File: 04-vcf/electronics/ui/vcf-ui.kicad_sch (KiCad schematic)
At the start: 39 parts, among them J1 Conn_02x03_Odd_Even, J2 Conn_02x02_Counter_Clockwise, J4 Conn_01x02, J5 Conn_01x06, J6 Conn_02x04_Odd_Even, U1 TL072

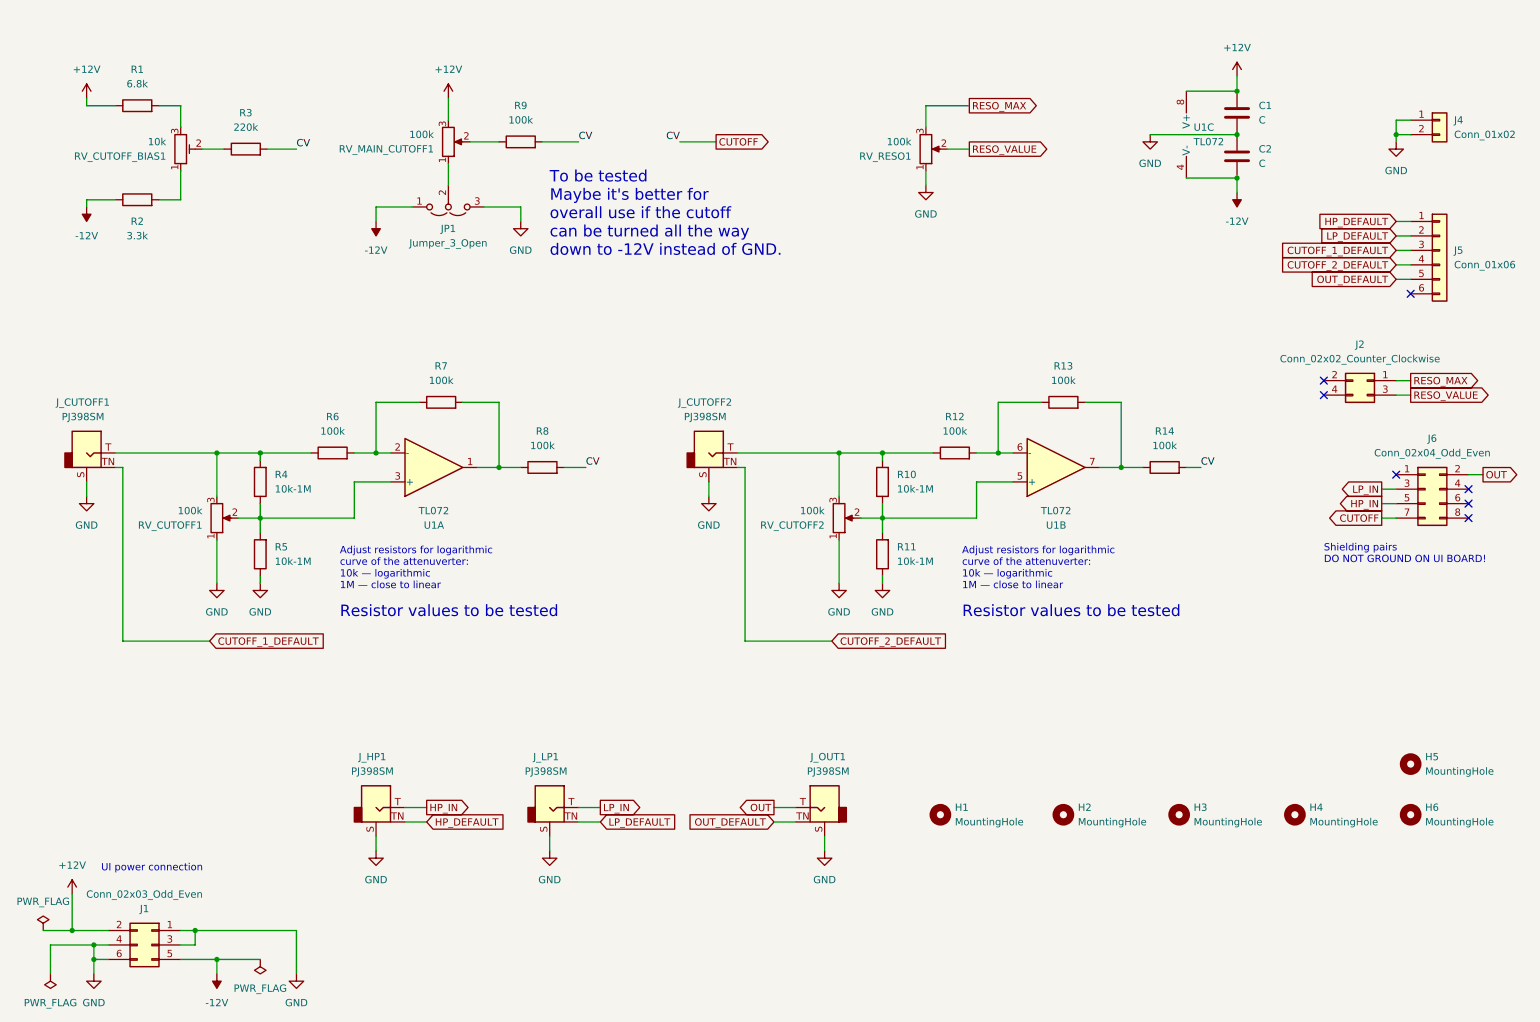
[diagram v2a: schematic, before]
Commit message: Fixed VCF v0.1 bugs - new version: v0.2
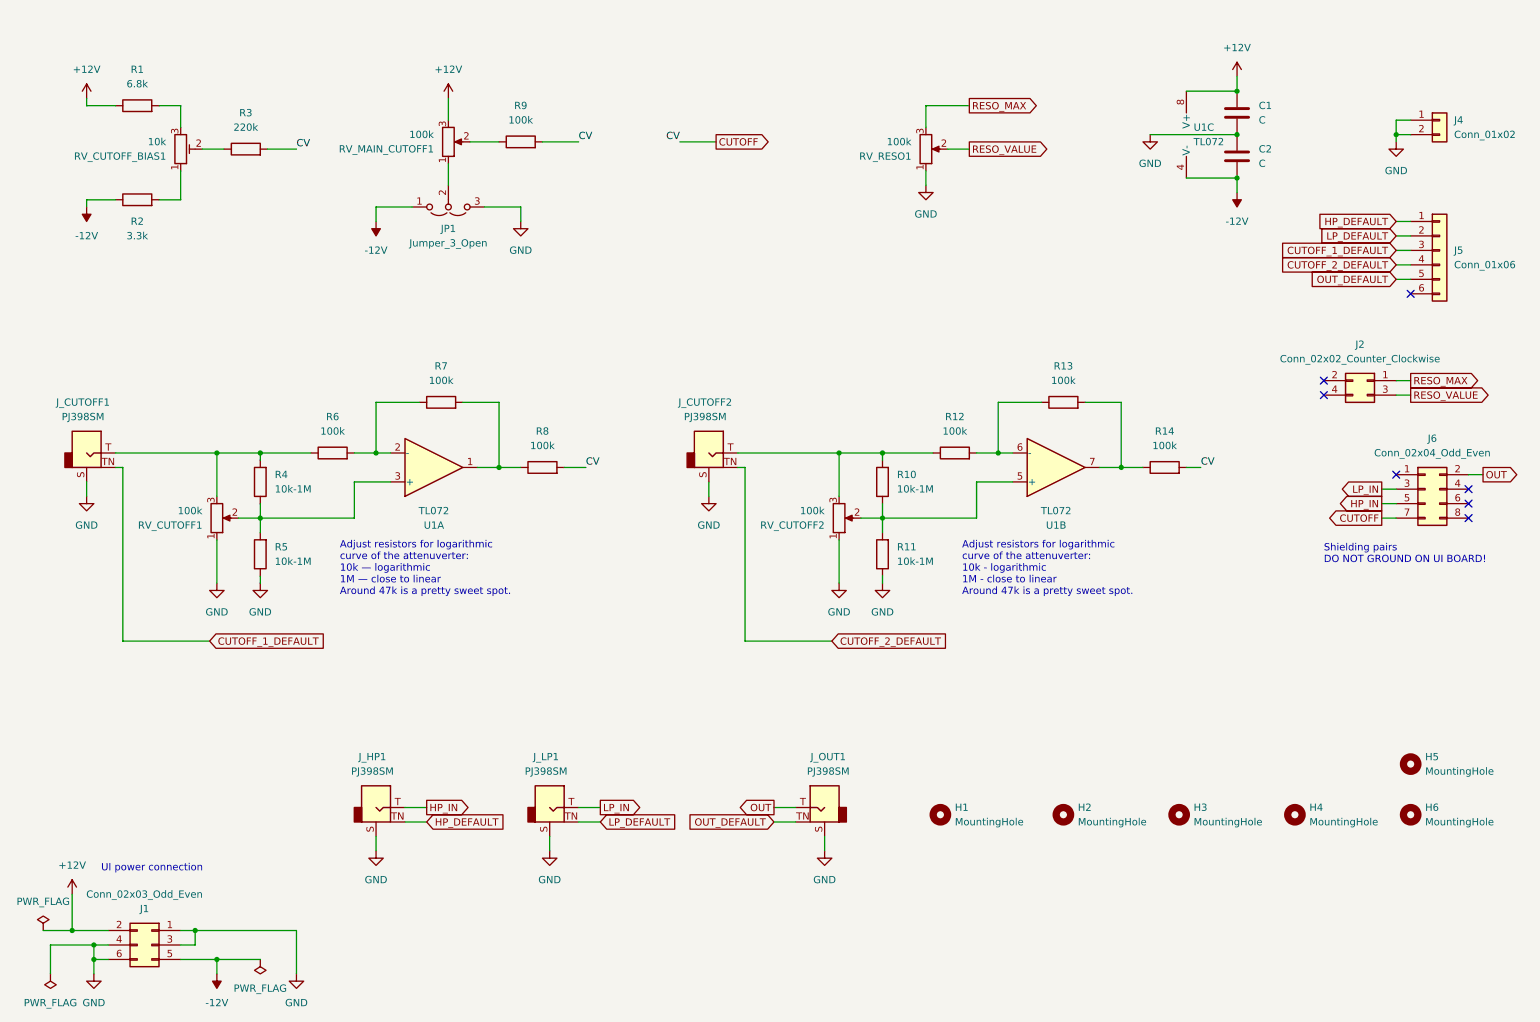
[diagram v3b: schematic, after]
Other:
- note added: "Adjust resistors for logarithmic curve of the attenuverter: 10k - logarithmic 1M - close to linear Around 47k is a pretty sweet spot."
- note added: "Adjust resistors for logarithmic curve of the attenuverter: 10k — logarithmic 1M — close to linear Around 47k is a pretty sweet spot."
- note removed: "Adjust resistors for logarithmic curve of the attenuverter: 10k — logarithmic 1M — close to linear"
- note removed: "Resistor values to be tested"
- note removed: "To be tested Maybe it's better for overall use if the cutoff can be turned all the way down to -12V instead of GND."
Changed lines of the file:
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@@
 		(title "Hog Moduleur VCO UI")
 		(date "2025-07-06")
-		(rev "v0.1")
+		(rev "v0.2")
 		(company "Shmøergh")
 	)
@@
 		)
 	)
-	(text "Adjust resistors for logarithmic\ncurve of the attenuverter: \n10k — logarithmic\n1M — close to linear"
+	(text "Adjust resistors for logarithmic\ncurve of the attenuverter: \n10k — logarithmic\n1M — close to linear\nAround 47k is a pretty sweet spot."
 		(exclude_from_sim no)
 		(at 73.66 116.84 0)
@@
 			(font
 				(size 1.27 1.27)
-			)
-			(justify left)
-		)
-	)
-	(text "To be tested\nMaybe it's better for\noverall use if the cutoff\ncan be turned all the way\ndown to -12V instead of GND."
-		(exclude_from_sim no)
-		(at 110.49 54.61 0)
-		(effects
-			(font
-				(size 2 2)
-				(thickness 0.25)
-				(color 255 0 255 1)
 			)
 			(justify left)
@@
 		)
 	)
-	(text "Resistor values to be tested"
-		(exclude_from_sim no)
-		(at 73.66 124.46 0)
-		(effects
-			(font
-				(size 2 2)
-				(thickness 0.25)
-				(color 255 0 255 1)
-			)
-			(justify left)
-		)
-	)
-	(text "Adjust resistors for logarithmic\ncurve of the attenuverter: \n10k — logarithmic\n1M — close to linear"
+	(text "Adjust resistors for logarithmic\ncurve of the attenuverter: \n10k - logarithmic\n1M - close to linear\nAround 47k is a pretty sweet spot."
 		(exclude_from_sim no)
 		(at 182.88 116.84 0)
@@
 			)
 			(justify left)
-		)
-	)
-	(text "Resistor values to be tested"
-		(exclude_from_sim no)
-		(at 182.88 124.46 0)
-		(effects
-			(font
-				(size 2 2)
-				(thickness 0.25)
-				(color 255 0 255 1)
-			)
-			(justify left)

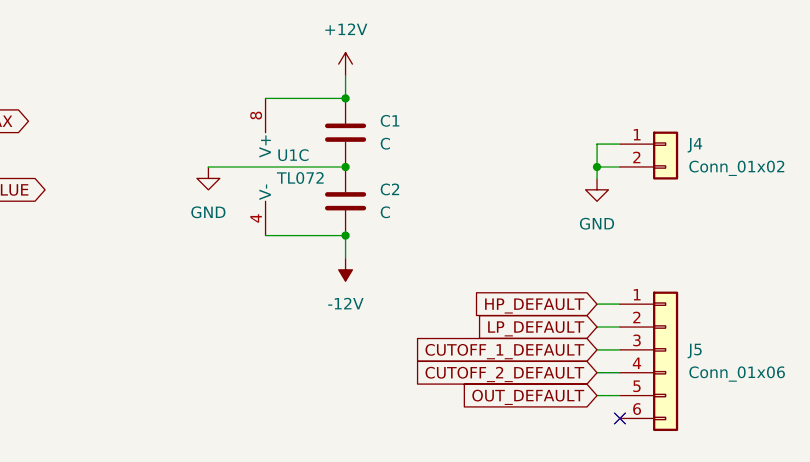
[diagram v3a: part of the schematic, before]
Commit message: Added combined PJ301 and PJ342 jack footprint
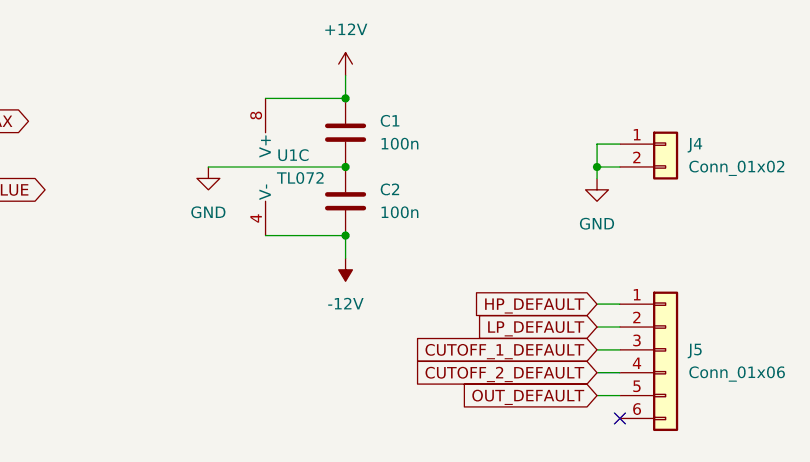
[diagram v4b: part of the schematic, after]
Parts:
- C1, C2: value C -> 100n
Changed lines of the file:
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@@
 			)
 		)
-		(property "Value" "C"
+		(property "Value" "100n"
 			(at 234.95 45.7199 0)
 			(effects
@@
 			)
 		)
-		(property "Value" "C"
+		(property "Value" "100n"
 			(at 234.95 38.0999 0)
 			(effects
